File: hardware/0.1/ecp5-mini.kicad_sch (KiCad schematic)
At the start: 22 parts, among them J3 S7 Mini, J4 S7 Mini, U1 ECP5U_12_CABGA256, X1 DSC6101CI2A-016

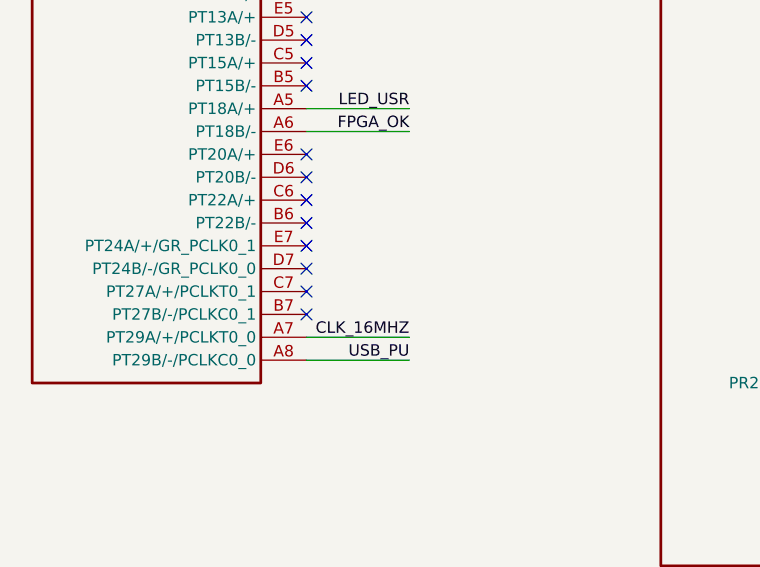
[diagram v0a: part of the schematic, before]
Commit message: move sd connector
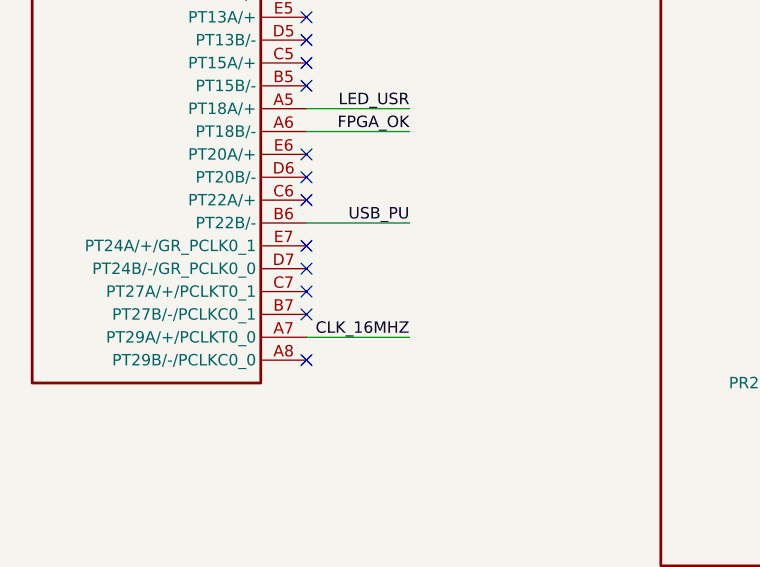
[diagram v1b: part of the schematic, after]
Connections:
- net USB_PU: now also U1.B6 (PT22B/-); no longer U1.A8 (PT29B/-/PCLKC0_0)
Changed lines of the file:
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@@
-(kicad_sch (version 20200820) (host eeschema "5.99.0-unknown-b0af66afc~103~ubuntu20.04.1")
+(kicad_sch (version 20200827) (generator eeschema)
   (page 1 5)
   (paper "A3")
+  (bus_alias "LED" (members "LED_[0..7]" "LED_R" "LED_G" "LED_B"))
+  (bus_alias "USB" (members "USB_D-" "USB_D+" "USB_PU"))
+  (bus_alias "HYPERRAM" (members "HR_nRST" "HR_nCS" "HR_CK_N" "HR_RWDS" "HR_DQ[0..7]" "HR_CK"))
   (bus_alias "SD" (members "SD_DAT[0..3]" "SD_CMD" "SD_CLK" "SD_DET"))
-  (bus_alias "HYPERRAM" (members "HR_nRST" "HR_nCS" "HR_CK_N" "HR_RWDS" "HR_DQ[0..7]" "HR_CK"))
-  (bus_alias "USB" (members "USB_D-" "USB_D+" "USB_PU"))
-  (bus_alias "LED" (members "LED_[0..7]" "LED_R" "LED_G" "LED_B"))
   (junction (at 60.96 63.5) (diameter 1.016) (color 0 0 0 0))
   (junction (at 62.23 177.8) (diameter 1.016) (color 0 0 0 0))
@@
   (junction (at 358.14 189.23) (diameter 1.016) (color 0 0 0 0))
   (junction (at 358.14 190.5) (diameter 1.016) (color 0 0 0 0))
+  (no_connect (at 208.28 217.17))
+  (no_connect (at 50.8 243.84))
+  (no_connect (at 50.8 106.68))
+  (no_connect (at 50.8 109.22))
+  (no_connect (at 50.8 91.44))
+  (no_connect (at 208.28 224.79))
+  (no_connect (at 130.81 266.7))
+  (no_connect (at 208.28 201.93))
+  (no_connect (at 130.81 274.32))
+  (no_connect (at 208.28 240.03))
+  (no_connect (at 130.81 220.98))
+  (no_connect (at 208.28 219.71))
+  (no_connect (at 50.8 93.98))
+  (no_connect (at 50.8 241.3))
+  (no_connect (at 50.8 101.6))
+  (no_connect (at 130.81 231.14))
+  (no_connect (at 50.8 198.12))
+  (no_connect (at 133.35 139.7))
+  (no_connect (at 130.81 236.22))
+  (no_connect (at 130.81 213.36))
+  (no_connect (at 133.35 109.22))
+  (no_connect (at 130.81 269.24))
+  (no_connect (at 208.28 260.35))
+  (no_connect (at 208.28 222.25))
+  (no_connect (at 208.28 242.57))
+  (no_connect (at 133.35 114.3))
+  (no_connect (at 208.28 227.33))
+  (no_connect (at 207.01 99.06))
+  (no_connect (at 130.81 271.78))
+  (no_connect (at 208.28 214.63))
+  (no_connect (at 50.8 231.14))
+  (no_connect (at 207.01 119.38))
+  (no_connect (at 208.28 199.39))
+  (no_connect (at 207.01 154.94))
+  (no_connect (at 50.8 200.66))
+  (no_connect (at 50.8 127))
+  (no_connect (at 50.8 116.84))
+  (no_connect (at 133.35 111.76))
+  (no_connect (at 50.8 96.52))
+  (no_connect (at 133.35 99.06))
+  (no_connect (at 50.8 99.06))
+  (no_connect (at 208.28 250.19))
+  (no_connect (at 133.35 106.68))
+  (no_connect (at 133.35 134.62))
+  (no_connect (at 207.01 116.84))
+  (no_connect (at 130.81 208.28))
+  (no_connect (at 208.28 262.89))
+  (no_connect (at 130.81 210.82))
+  (no_connect (at 133.35 137.16))
+  (no_connect (at 208.28 252.73))
+  (no_connect (at 207.01 96.52))
+  (no_connect (at 207.01 149.86))
+  (no_connect (at 50.8 104.14))
+  (no_connect (at 207.01 160.02))
+  (no_connect (at 50.8 220.98))
+  (no_connect (at 50.8 238.76))
+  (no_connect (at 208.28 232.41))
+  (no_connect (at 208.28 245.11))
+  (no_connect (at 130.81 233.68))
+  (no_connect (at 208.28 247.65))
+  (no_connect (at 130.81 205.74))
+  (no_connect (at 50.8 208.28))
+  (no_connect (at 50.8 129.54))
+  (no_connect (at 208.28 209.55))
+  (no_connect (at 208.28 212.09))
+  (no_connect (at 50.8 236.22))
+  (no_connect (at 207.01 93.98))
   (no_connect (at 207.01 157.48))
-  (no_connect (at 208.28 227.33))
-  (no_connect (at 130.81 233.68))
-  (no_connect (at 208.28 224.79))
-  (no_connect (at 207.01 99.06))
+  (no_connect (at 50.8 195.58))
+  (no_connect (at 207.01 147.32))
+  (no_connect (at 130.81 261.62))
+  (no_connect (at 133.35 96.52))
+  (no_connect (at 207.01 91.44))
+  (no_connect (at 130.81 223.52))
+  (no_connect (at 130.81 264.16))
+  (no_connect (at 50.8 218.44))
+  (no_connect (at 208.28 229.87))
   (no_connect (at 50.8 119.38))
-  (no_connect (at 50.8 198.12))
-  (no_connect (at 50.8 106.68))
-  (no_connect (at 130.81 208.28))
-  (no_connect (at 50.8 231.14))
+  (no_connect (at 207.01 152.4))
   (no_connect (at 133.35 132.08))
-  (no_connect (at 130.81 266.7))
-  (no_connect (at 130.81 261.62))
-  (no_connect (at 208.28 212.09))
-  (no_connect (at 208.28 201.93))
-  (no_connect (at 133.35 111.76))
-  (no_connect (at 208.28 222.25))
-  (no_connect (at 208.28 262.89))
-  (no_connect (at 50.8 109.22))
-  (no_connect (at 50.8 124.46))
-  (no_connect (at 133.35 114.3))
-  (no_connect (at 207.01 91.44))
-  (no_connect (at 133.35 139.7))
-  (no_connect (at 133.35 137.16))
-  (no_connect (at 50.8 93.98))
-  (no_connect (at 208.28 252.73))
-  (no_connect (at 50.8 127))
-  (no_connect (at 133.35 99.06))
-  (no_connect (at 208.28 214.63))
   (no_connect (at 50.8 121.92))
-  (no_connect (at 207.01 116.84))
-  (no_connect (at 50.8 101.6))
-  (no_connect (at 208.28 219.71))
-  (no_connect (at 130.81 213.36))
-  (no_connect (at 207.01 96.52))
-  (no_connect (at 50.8 129.54))
-  (no_connect (at 207.01 154.94))
-  (no_connect (at 50.8 236.22))
-  (no_connect (at 130.81 220.98))
-  (no_connect (at 130.81 223.52))
-  (no_connect (at 207.01 149.86))
-  (no_connect (at 207.01 147.32))
-  (no_connect (at 130.81 264.16))
-  (no_connect (at 133.35 109.22))
-  (no_connect (at 208.28 209.55))
-  (no_connect (at 208.28 250.19))
-  (no_connect (at 130.81 236.22))
-  (no_connect (at 207.01 119.38))
-  (no_connect (at 50.8 91.44))
-  (no_connect (at 50.8 200.66))
-  (no_connect (at 50.8 96.52))
-  (no_connect (at 207.01 93.98))
-  (no_connect (at 208.28 229.87))
-  (no_connect (at 130.81 269.24))
-  (no_connect (at 207.01 160.02))
-  (no_connect (at 50.8 243.84))
-  (no_connect (at 50.8 195.58))
-  (no_connect (at 208.28 260.35))
-  (no_connect (at 50.8 238.76))
-  (no_connect (at 130.81 231.14))
-  (no_connect (at 50.8 241.3))
-  (no_connect (at 50.8 116.84))
-  (no_connect (at 208.28 217.17))
-  (no_connect (at 130.81 205.74))
-  (no_connect (at 208.28 247.65))
-  (no_connect (at 50.8 218.44))
-  (no_connect (at 208.28 199.39))
-  (no_connect (at 130.81 274.32))
-  (no_connect (at 133.35 134.62))
-  (no_connect (at 50.8 208.28))
-  (no_connect (at 50.8 220.98))
+  (no_connect (at 50.8 139.7))
   (no_connect (at 50.8 132.08))
-  (no_connect (at 50.8 104.14))
-  (no_connect (at 133.35 106.68))
-  (no_connect (at 208.28 240.03))
-  (no_connect (at 208.28 242.57))
-  (no_connect (at 208.28 245.11))
-  (no_connect (at 130.81 210.82))
   (no_connect (at 50.8 134.62))
-  (no_connect (at 50.8 99.06))
-  (no_connect (at 133.35 96.52))
-  (no_connect (at 207.01 152.4))
-  (no_connect (at 130.81 271.78))
-  (no_connect (at 208.28 232.41))
   (bus_entry (at 62.23 203.2) (size 2.54 -2.54)
     (stroke (width 0.1524) (type solid) (color 0 0 0 0))
@@
     (stroke (width 0) (type solid) (color 0 0 0 0))
   )
-  (wire (pts (xy 50.8 139.7) (xy 62.23 139.7))
+  (wire (pts (xy 50.8 124.46) (xy 62.23 124.46))
     (stroke (width 0) (type solid) (color 0 0 0 0))
   )
@@
     (effects (font (size 1.27 1.27)) (justify right bottom))
   )
+  (label "USB_PU" (at 62.23 124.46 180)
+    (effects (font (size 1.27 1.27)) (justify right bottom))
+  )
   (label "CLK_16MHZ" (at 62.23 137.16 180)
     (effects (font (size 1.27 1.27)) (justify right bottom))
   )
-  (label "USB_PU" (at 62.23 139.7 180)
-    (effects (font (size 1.27 1.27)) (justify right bottom))
-  )

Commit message: update readme
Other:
- moved on the sheet: C14, X1

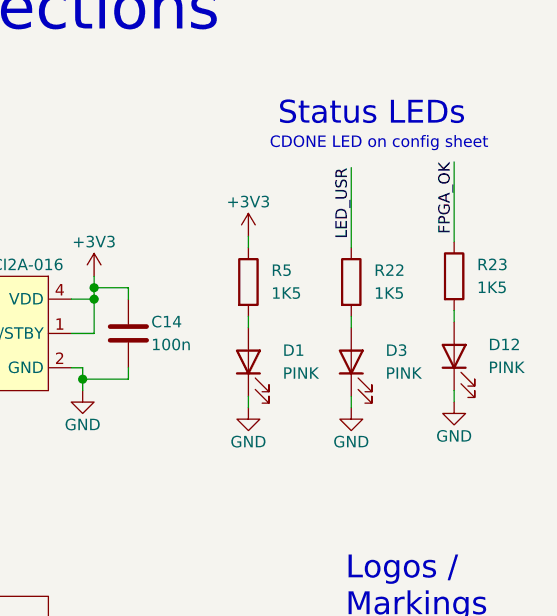
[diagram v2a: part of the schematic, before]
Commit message: adding silk
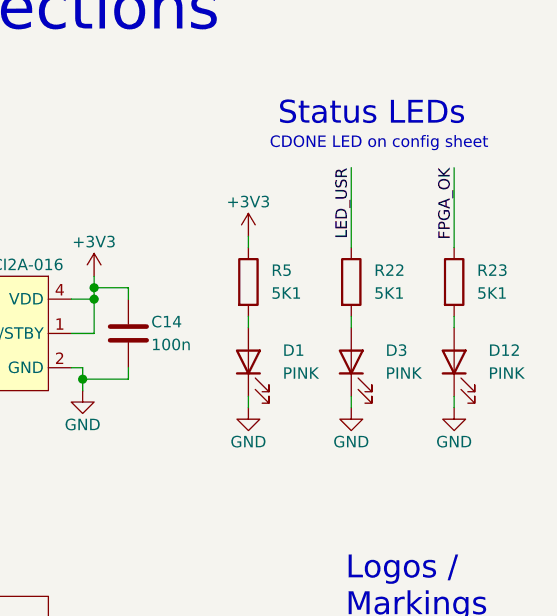
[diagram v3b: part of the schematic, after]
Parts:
- J3, J4, LOGO1, LOGO2: DNP (none) -> DNP
- R22, R23, R5: value 1K5 -> 5K1
- U1: manf# ECP5U_12 -> (none)
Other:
- moved on the sheet: D12, R23

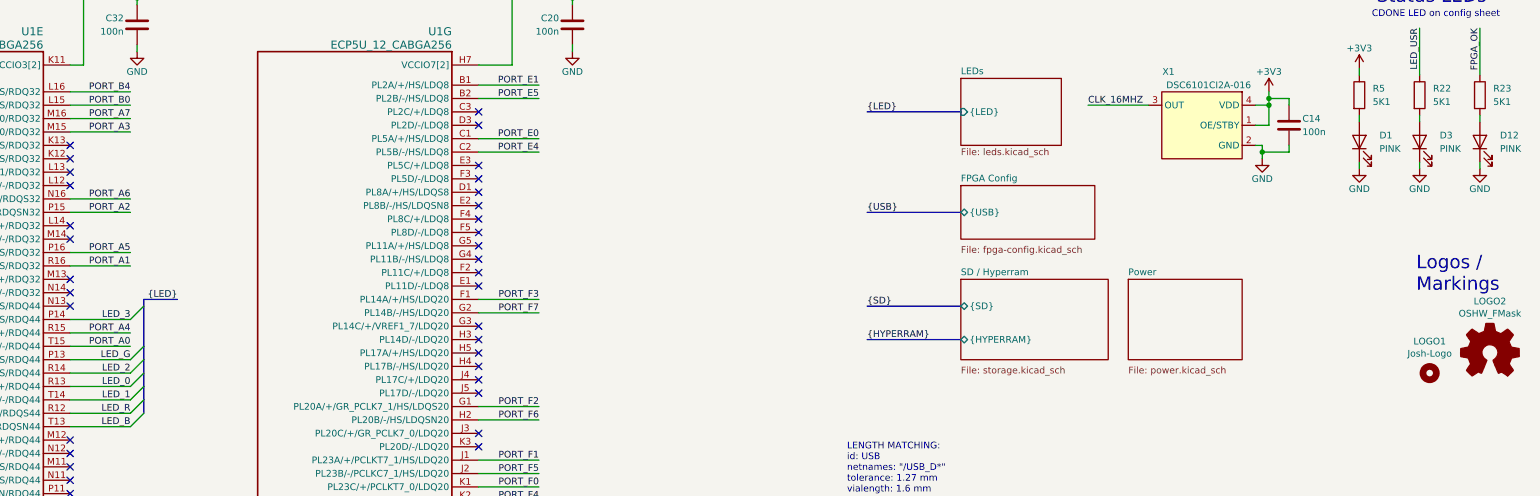
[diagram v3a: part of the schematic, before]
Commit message: change LEDs, optimise parts
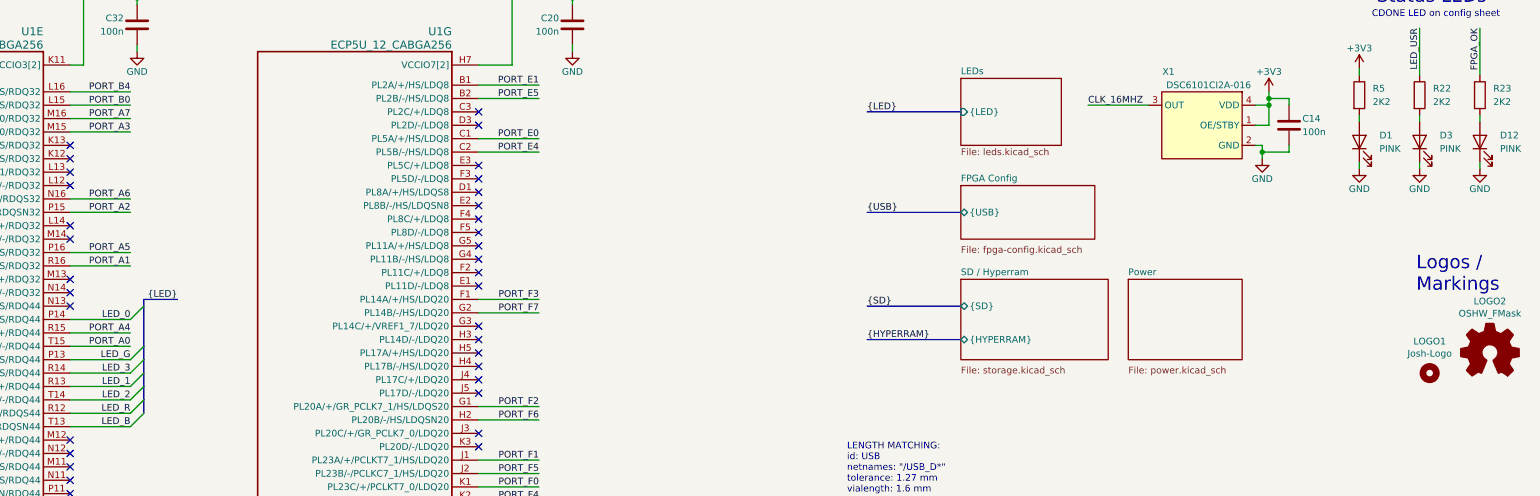
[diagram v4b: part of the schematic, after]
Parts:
- R22, R23, R5: value 5K1 -> 2K2
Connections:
- net LED_0: now also U1.P14 (PR38B/-/HS/RDQ44); no longer U1.R13 (PR41C/+/RDQ44)
- net LED_1: now also U1.R13 (PR41C/+/RDQ44); no longer U1.T14 (PR41D/-/RDQ44)
- net LED_2: now also U1.T14 (PR41D/-/RDQ44); no longer U1.R14 (PR41B/-/HS/RDQ44)
- net LED_3: now also U1.R14 (PR41B/-/HS/RDQ44); no longer U1.P14 (PR38B/-/HS/RDQ44)

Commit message: add part numbers
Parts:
- C14, C19, C20, C25, C26, C31, C32: LCSC (none) -> C1525; MPN (none) -> CL05B104KO5NNNC; Manufacturer (none) -> Samsung Electro-Mechanics
- C23, C29, C30: LCSC (none) -> C368809; MPN (none) -> CL05A475KP5NRNC; Manufacturer (none) -> Samsung Electro-Mechanics
- D1, D12, D3: LCSC (none) -> C268294; MPN (none) -> OSK40603C1E; Manufacturer (none) -> OptoSupply
- R22, R23, R5: LCSC (none) -> C25933; MPN (none) -> 0402WGJ0222TCE; Manufacturer (none) -> UNI-ROYAL(Uniroyal Elec)
- U1: MPN (none) -> LFE5U-12F-8BG256C; Manufacturer (none) -> Lattice; Mouser (none) -> 842-LFE5U12F8BG256C
- X1: MPN DSC6101CI1A-012.0000T -> DSC6101CI2A-016.0000; Manufacturer (none) -> Microchip Technology; Mouser (none) -> 579-101CI2A0160000

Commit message: design review done
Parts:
- U1: MPN LFE5U-12F-8BG256C -> LFE5U12F8BG256C
- X1: Manufacturer Microchip Technology -> Microchip

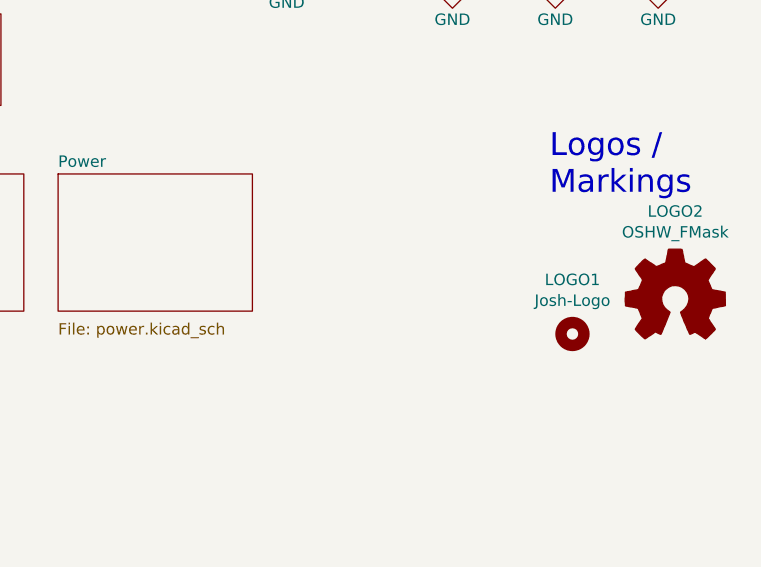
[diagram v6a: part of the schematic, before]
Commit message: add fiducals
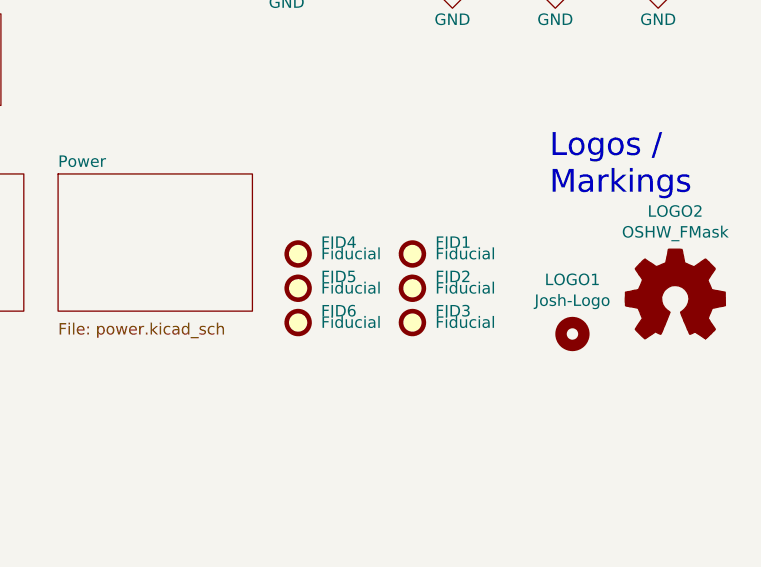
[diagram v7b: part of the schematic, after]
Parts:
- added FID1, FID2, FID3, FID4, FID5, FID6: Fiducial, Fiducial:Fiducial_0.75mm_Mask1.5mm, symbol Mechanical:Fiducial

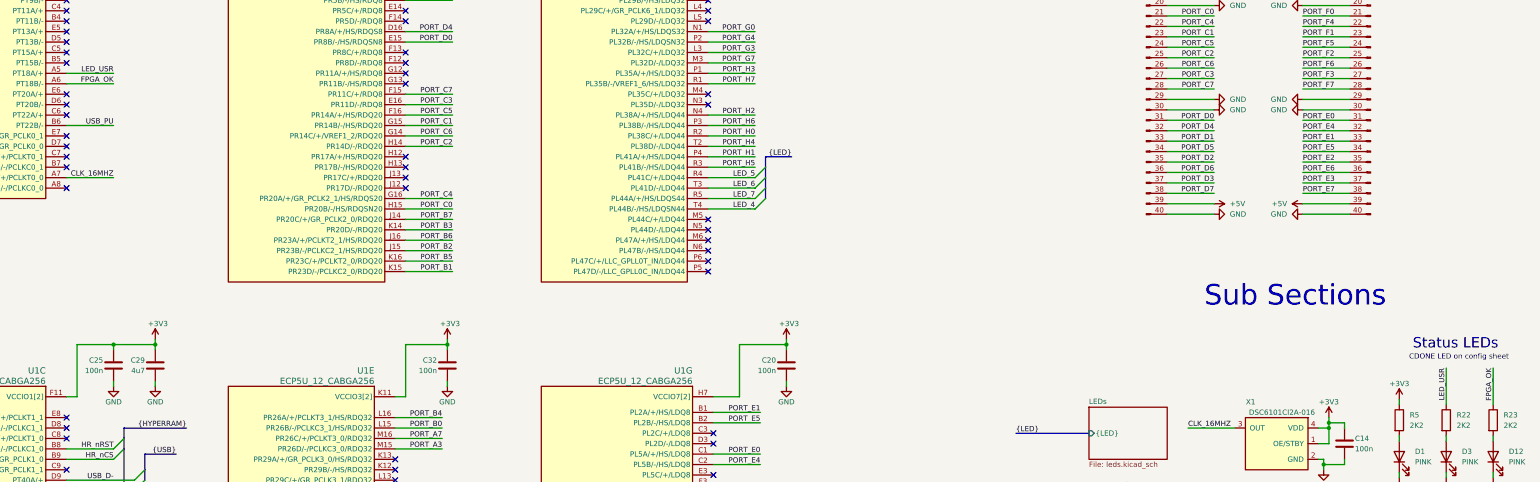
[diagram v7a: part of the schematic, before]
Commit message: set clearances to a more reasonable number
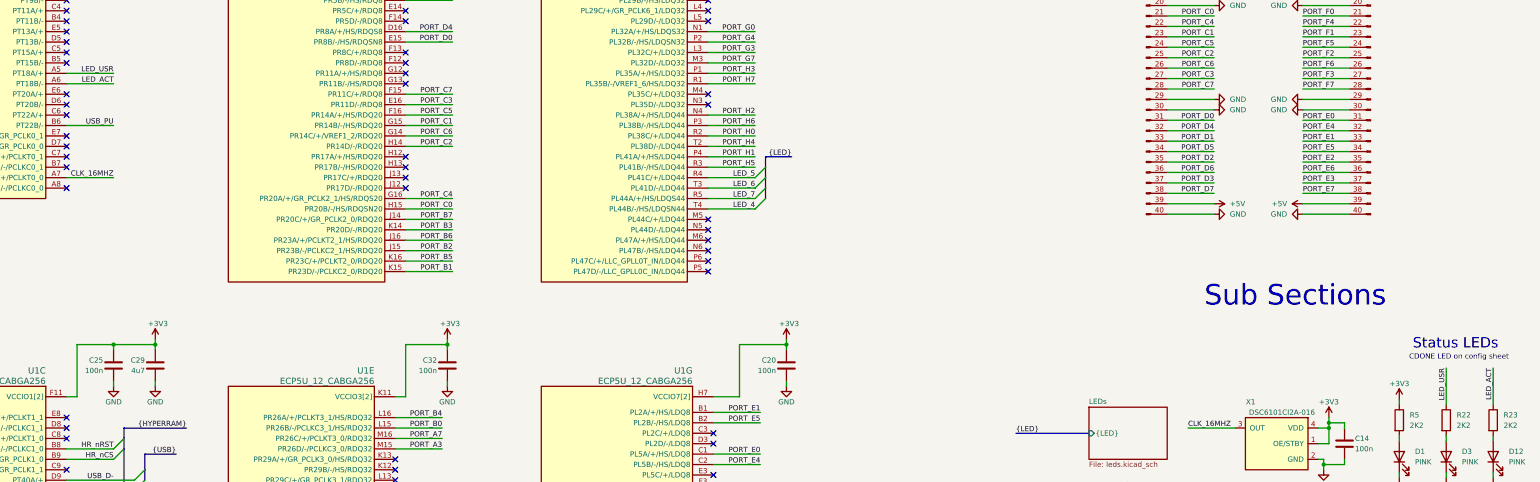
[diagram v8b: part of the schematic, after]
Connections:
- net FPGA_OK renamed LED_ACT
